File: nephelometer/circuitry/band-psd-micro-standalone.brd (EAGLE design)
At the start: 88 x 54 mm, 68 parts, among them IC1 LMC6484P, IC2 LM555N, IC3 74HCT74N, IC4 4044N, IC8 7805TV, T1 2N2222, T2 2N2222, U1 MAX4544, U4 MotA

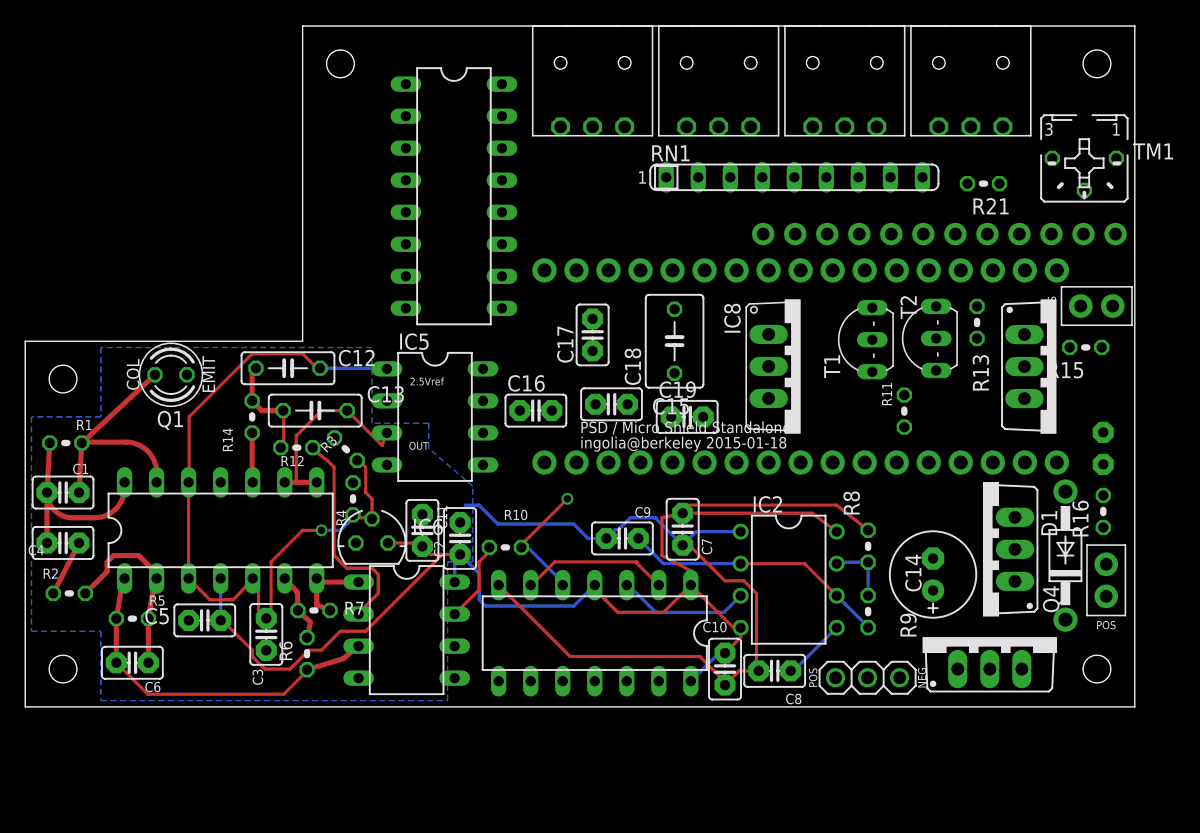
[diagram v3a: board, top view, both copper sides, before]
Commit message: Better wiring for push-buttons (to PCINT pins) and LCD (allow INT)
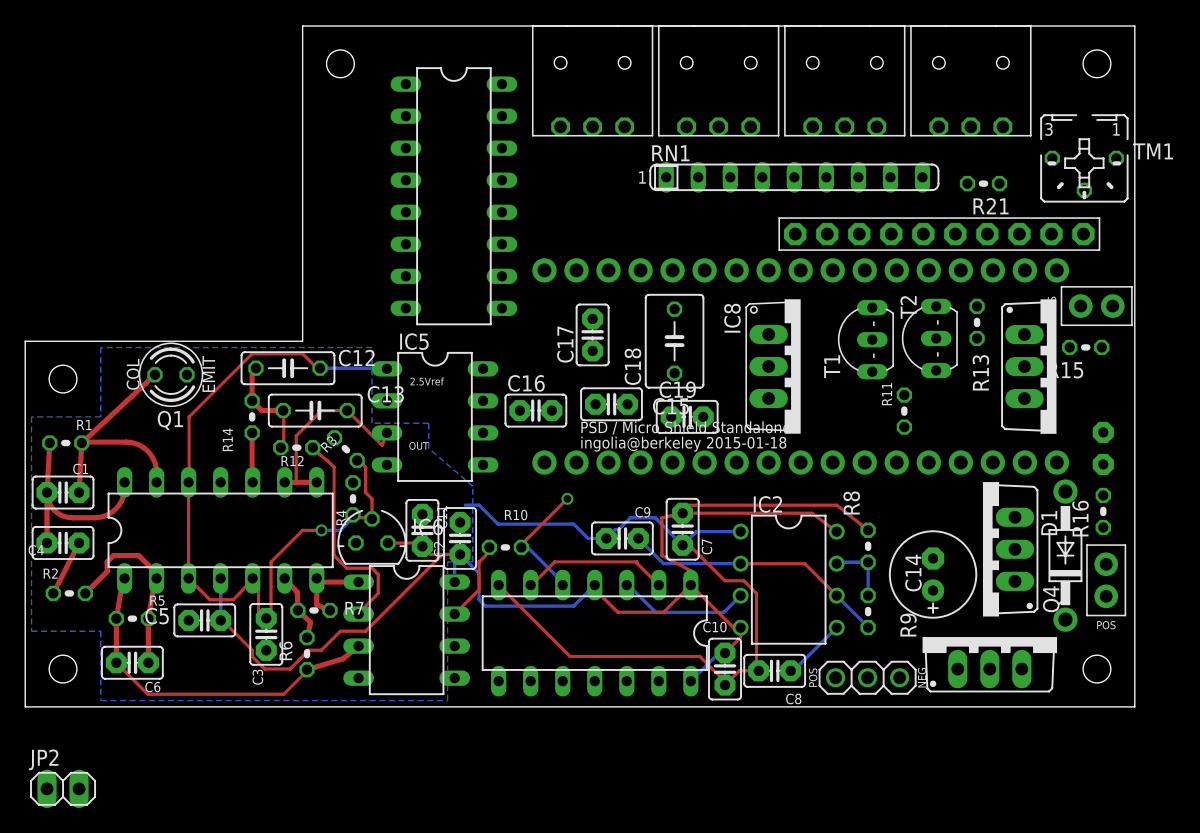
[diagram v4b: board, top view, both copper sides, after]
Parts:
- added JP2: (no value), pinhead:1X02
- 16X2: value (none) -> PINHD-1X10; device adafruit:1X12-CB -> adafruit:1X10-BIG
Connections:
- new net N$11: IC4.9, U3.P$2
- new net N$15: IC4.13, U3.P$1
- new net N$21: JP2.1, R21.1
- new net N$24: 16X2.10, U3.P$5
- new net N$29: 16X2.9, U3.P$6
- new net N$30: 16X2.8, U3.P$7
- new net N$46: 16X2.4, U3.P$11
- net GND: now also JP2.2; no longer 16X2.12
- net N$31: now also 16X2.7, U3.P$8; no longer IC4.13, U3.P$10
- net N$32: now also 16X2.6, U3.P$9; no longer IC4.9, U3.P$11
- net N$39: now also U3.P$4; no longer U3.P$15
- net N$41: now also 16X2.5, U3.P$10; no longer 16X2.11, R21.1
- net N$45: now also U3.P$3; no longer U3.P$14
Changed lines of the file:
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@@
 <attribute name="VALUE" x="43.786" y="30.794" size="1.27" layer="27" ratio="10" rot="R180"/>
 </element>
-<element name="16X2" library="adafruit" package="1X12-CB" value="" x="72.5" y="43.5" smashed="yes">
+<element name="16X2" library="adafruit" package="1X10-BIG" value="PINHD-1X10" x="72.5" y="43.5" smashed="yes">
 <attribute name="NAME" x="72.6838" y="44.8288" size="1.27" layer="22" ratio="10" rot="MR0" align="bottom-center"/>
 <attribute name="VALUE" x="57.26" y="40.325" size="1.27" layer="27"/>
@@
 <element name="IC8" library="linear" package="TO220V" value="7805TV" x="61.5" y="33" rot="R270"/>
 <element name="C19" library="adafruit" package="C025-025X050" value="0.33µ" x="52.5" y="29"/>
+<element name="JP2" library="pinhead" package="1X02" value="" x="3" y="-0.5"/>
 </elements>
 <signals>
@@
 <contactref element="IC8" pad="3"/>
 <contactref element="C19" pad="1"/>
-<wire x1="63.61" y1="43.5" x2="74.73" y2="47.5" width="0" layer="19" extent="1-1"/>
-<wire x1="50.84" y1="48" x2="63.61" y2="43.5" width="0" layer="19" extent="1-1"/>
+<wire x1="66.15" y1="43.5" x2="74.73" y2="47.5" width="0" layer="19" extent="1-1"/>
+<wire x1="50.84" y1="48" x2="66.15" y2="43.5" width="0" layer="19" extent="1-1"/>
 <wire x1="86.54" y1="49.5" x2="50.84" y2="48" width="0" layer="19" extent="1-1"/>
 <wire x1="47.77" y1="30" x2="86.54" y2="49.5" width="0" layer="19" extent="1-1"/>
@@
 <contactref element="TM1" pad="E"/>
 <contactref element="16X2" pad="1"/>
-<contactref element="16X2" pad="12"/>
 <contactref element="U$6" pad="P$2"/>
 <contactref element="U$5" pad="P$2"/>
@@
 <contactref element="R4" pad="1"/>
 <contactref element="C3" pad="2"/>
+<contactref element="JP2" pad="2"/>
 <wire x1="75" y1="52" x2="81.46" y2="49.5" width="0" layer="19" extent="1-1"/>
-<wire x1="86.47" y1="43.5" x2="81.46" y2="49.5" width="0" layer="19" extent="1-1"/>
-<wire x1="85.38" y1="34.51" x2="86.47" y2="43.5" width="0" layer="19" extent="1-1"/>
 <wire x1="65" y1="52" x2="75" y2="52" width="0" layer="19" extent="1-1"/>
+<wire x1="61.07" y1="43.5" x2="65" y2="52" width="0" layer="19" extent="1-1"/>
 <wire x1="55" y1="52" x2="65" y2="52" width="0" layer="19" extent="1-1"/>
-<wire x1="58.53" y1="43.5" x2="55" y2="52" width="0" layer="19" extent="1-1"/>
-<wire x1="51.5" y1="37.54" x2="58.53" y2="43.5" width="0" layer="19" extent="1-1"/>
+<wire x1="45" y1="52" x2="55" y2="52" width="0" layer="19" extent="1-1"/>
+<wire x1="51.5" y1="37.54" x2="61.07" y2="43.5" width="0" layer="19" extent="1-1"/>
 <wire x1="45" y1="36.77" x2="51.5" y2="37.54" width="0" layer="19" extent="1-1"/>
 <wire x1="45.23" y1="30" x2="45" y2="36.77" width="0" layer="19" extent="1-1"/>
@@
 <wire x1="26" y1="23.77" x2="28.69" y2="25.19" width="0" layer="19" extent="1-1"/>
 <wire x1="53.77" y1="29" x2="48.8" y2="25.38" width="0" layer="19" extent="1-1"/>
-<wire x1="45" y1="52" x2="55" y2="52" width="0" layer="19" extent="1-1"/>
 <wire x1="15.5" y1="23.81" x2="26" y2="23.77" width="0" layer="19" extent="1-1"/>
 <wire x1="12.83" y1="32.34" x2="15.5" y2="23.81" width="0" layer="19" extent="1-1"/>
@@
 <wire x1="19.12" y1="10.48" x2="12.97" y2="12.86" width="0" layer="19" extent="1-1"/>
 <wire x1="26.44" y1="8.28" x2="19.12" y2="10.48" width="0" layer="19" extent="1-1"/>
+<wire x1="67.18" y1="32.58" x2="61.07" y2="43.5" width="0" layer="19" extent="1-1"/>
+<wire x1="72.25" y1="32.68" x2="67.18" y2="32.58" width="0" layer="19" extent="1-1"/>
 <wire x1="30.19" y1="37.61" x2="28.69" y2="25.19" width="0" layer="19" extent="1-1"/>
-<wire x1="72.25" y1="32.68" x2="85.38" y2="34.51" width="0" layer="19" extent="1-1"/>
-<wire x1="67.18" y1="32.58" x2="72.25" y2="32.68" width="0" layer="19" extent="1-1"/>
 <wire x1="78.5" y1="21.04" x2="72.25" y2="32.68" width="0" layer="19" extent="1-1"/>
 <wire x1="85.5" y1="20.23" x2="78.5" y2="21.04" width="0" layer="19" extent="1-1"/>
 <wire x1="72" y1="17.77" x2="78.5" y2="21.04" width="0" layer="19" extent="1-1"/>
 <wire x1="76.5" y1="9" x2="72" y2="17.77" width="0" layer="19" extent="1-1"/>
+<wire x1="85.38" y1="34.51" x2="72.25" y2="32.68" width="0" layer="19" extent="1-1"/>
+<wire x1="4.27" y1="-0.5" x2="12.97" y2="12.86" width="0" layer="19" extent="1-1"/>
 </signal>
 <signal name="N$4">
@@
 <wire x1="78.5" y1="15.96" x2="81.82" y2="25.38" width="0" layer="19" extent="1-1"/>
 </signal>
-<signal name="N$31">
-<contactref element="U3" pad="P$10"/>
-<contactref element="IC4" pad="13"/>
-<wire x1="37.81" y1="47.77" x2="58.96" y2="40.62" width="0" layer="19" extent="1-1"/>
-</signal>
-<signal name="N$32">
-<contactref element="U3" pad="P$11"/>
-<contactref element="IC4" pad="9"/>
-<wire x1="37.81" y1="37.61" x2="56.42" y2="40.62" width="0" layer="19" extent="1-1"/>
-</signal>
 <signal name="N$38">
 <contactref element="16X2" pad="2"/>
 <contactref element="TM1" pad="S"/>
-<wire x1="84" y1="46.96" x2="61.07" y2="43.5" width="0" layer="19" extent="1-1"/>
-</signal>
-<signal name="N$41">
-<contactref element="R21" pad="1"/>
-<contactref element="16X2" pad="11"/>
-<wire x1="83.93" y1="43.5" x2="77.27" y2="47.5" width="0" layer="19" extent="1-1"/>
+<wire x1="84" y1="46.96" x2="63.61" y2="43.5" width="0" layer="19" extent="1-1"/>
 </signal>
 <signal name="MISO">
@@
 <signal name="N$39">
 <contactref element="IC4" pad="1"/>
-<contactref element="U3" pad="P$15"/>
-<wire x1="30.19" y1="55.39" x2="46.26" y2="40.62" width="0" layer="19" extent="1-1"/>
+<contactref element="U3" pad="P$4"/>
+<wire x1="30.19" y1="55.39" x2="74.2" y2="40.62" width="0" layer="19" extent="1-1"/>
 </signal>
 <signal name="N$45">
-<contactref element="U3" pad="P$14"/>
 <contactref element="IC4" pad="10"/>
-<wire x1="37.81" y1="40.15" x2="48.8" y2="40.62" width="0" layer="19" extent="1-1"/>
+<contactref element="U3" pad="P$3"/>
+<wire x1="37.81" y1="40.15" x2="76.74" y2="40.62" width="0" layer="19" extent="1-1"/>
 </signal>
 <signal name="N$35">
@@
 <wire x1="2.23" y1="15" x2="4.27" y2="19" width="0.4064" layer="1"/>
 </signal>
+<signal name="N$11">
+<contactref element="U3" pad="P$2"/>
+<contactref element="IC4" pad="9"/>
+<wire x1="37.81" y1="37.61" x2="79.28" y2="40.62" width="0" layer="19" extent="1-1"/>
+</signal>
+<signal name="N$15">
+<contactref element="IC4" pad="13"/>
+<contactref element="U3" pad="P$1"/>
+<wire x1="37.81" y1="47.77" x2="81.82" y2="40.62" width="0" layer="19" extent="1-1"/>
+</signal>
+<signal name="N$21">
+<contactref element="R21" pad="1"/>
+<contactref element="JP2" pad="1"/>
+<wire x1="1.73" y1="-0.5" x2="77.27" y2="47.5" width="0" layer="19" extent="1-1"/>
+</signal>
+<signal name="N$24">
+<contactref element="U3" pad="P$5"/>
+<contactref element="16X2" pad="10"/>
+<wire x1="71.66" y1="40.62" x2="83.93" y2="43.5" width="0" layer="19" extent="1-1"/>
+</signal>
+<signal name="N$29">
+<contactref element="16X2" pad="9"/>
+<contactref element="U3" pad="P$6"/>
+<wire x1="69.12" y1="40.62" x2="81.39" y2="43.5" width="0" layer="19" extent="1-1"/>
+</signal>
+<signal name="N$30">
+<contactref element="U3" pad="P$7"/>
+<contactref element="16X2" pad="8"/>
+<wire x1="66.58" y1="40.62" x2="78.85" y2="43.5" width="0" layer="19" extent="1-1"/>
+</signal>
+<signal name="N$31">
+<contactref element="U3" pad="P$8"/>
+<contactref element="16X2" pad="7"/>
+<wire x1="64.04" y1="40.62" x2="76.31" y2="43.5" width="0" layer="19" extent="1-1"/>
+</signal>
+<signal name="N$32">
+<contactref element="U3" pad="P$9"/>
+<contactref element="16X2" pad="6"/>
+<wire x1="61.5" y1="40.62" x2="73.77" y2="43.5" width="0" layer="19" extent="1-1"/>
+</signal>
+<signal name="N$41">
+<contactref element="U3" pad="P$10"/>
+<contactref element="16X2" pad="5"/>
+<wire x1="58.96" y1="40.62" x2="71.23" y2="43.5" width="0" layer="19" extent="1-1"/>
+</signal>
+<signal name="N$46">
+<contactref element="U3" pad="P$11"/>
+<contactref element="16X2" pad="4"/>
+<wire x1="56.42" y1="40.62" x2="68.69" y2="43.5" width="0" layer="19" extent="1-1"/>
+</signal>
 </signals>

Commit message: Started routing power supply
Started part numbers for filter components
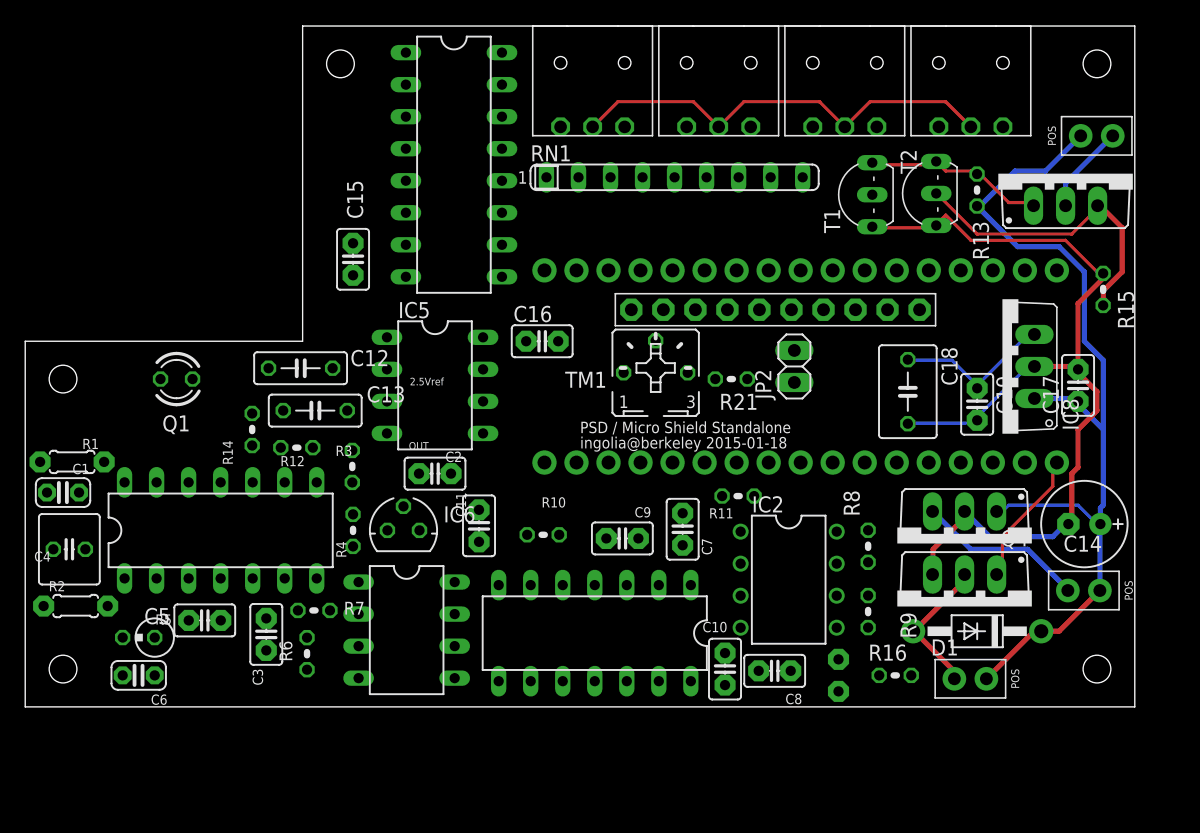
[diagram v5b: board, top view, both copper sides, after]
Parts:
- C1: value 2n -> 2.2nF; device adafruit:C025-025X050 -> adafruit:C025-024X044
- C4: device adafruit:C025-025X050 -> adafruit:C025-060X050
- C6: device adafruit:C025-025X050 -> adafruit:C025-024X044
- Q1: device ingolia:PTRANS -> ingolia:3MM_LED
- R1, R2: device adafruit:0204V -> adafruit:0204/5
- R5: device adafruit:0204V -> adafruit:0309V
- U2: device ingolia:3WIRES -> ingolia:1X02_SCREW
- moved JP2 67.0 mm to (61.0, 33.0), turned to 90 degrees
- moved C17 38.7 mm to (83.5, 31.5)
- moved TM1 38.0 mm to (50.0, 32.5), turned to 0 degrees
- moved LED1 27.7 mm to (64.5, 8.50)
- moved U2 26.4 mm to (86.5, 16.5), turned to 180 degrees
- moved R21 25.3 mm to (56.0, 32.0)
- moved C15 23.5 mm to (26.0, 41.5), turned to 270 degrees
- moved C19 23.0 mm to (75.5, 30.0), turned to 270 degrees
- moved R16 21.0 mm to (69.0, 8.50), turned to 0 degrees
- moved C18 18.9 mm to (70.0, 31.0), turned to 270 degrees
- moved IC8 16.0 mm to (77.5, 33.0), turned to 90 degrees
- moved R11 14.8 mm to (56.5, 22.7), turned to 180 degrees
- moved 16X2 14.3 mm to (59.5, 37.5)
- moved JP1 13.5 mm to (82.4, 50.0)
- moved Q2 13.2 mm to (82.5, 45.8), turned to 0 degrees
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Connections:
- removed net GNDBREAK: U2.2-DETECT
- net +12V: now also U2.1/POS; no longer U2.1-POS
- net GND: now also IC8.2
- net N$47: now also U2.2; no longer U2.3-NEG
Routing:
- net +5V: track 107.4 -> 13.4 mm
- net +12V: track 0.00 -> 74.8 mm
- net 2.5V: track 59.5 -> 0.00 mm, vias 1 -> 0
- net GND: track 63.4 -> 109.6 mm
- net N$26: track 28.4 -> 0.00 mm
- net N$14: track 0.00 -> 24.6 mm
- net N$9: track 21.2 -> 0.00 mm
- net N$1: track 19.6 -> 0.00 mm
- net N$6: track 17.2 -> 0.00 mm
- net N$22: track 16.3 -> 0.00 mm
- net N$28: track 16.1 -> 0.00 mm
- net N$25: track 15.1 -> 0.00 mm
- net N$8: track 0.00 -> 14.6 mm
- net N$47: track 0.00 -> 13.4 mm
- net N$12: track 11.7 -> 0.00 mm
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- removed copper zone on layer 16, net GND

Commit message: Specific parts for all analog components
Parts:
- C12: device adafruit:C050-025X075 -> adafruit:C025-024X044
- C13: value 50nF -> 47nF; device adafruit:C050-025X075 -> adafruit:C025-040X050
- C2, C4, C5: value 100n -> 100nF
- C3: device adafruit:C025-025X050 -> adafruit:C050-024X044
- C6: value 10p -> 10pF
